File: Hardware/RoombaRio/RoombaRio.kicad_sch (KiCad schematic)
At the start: 1 part, among them J101 Raspberry_Pi_2_3

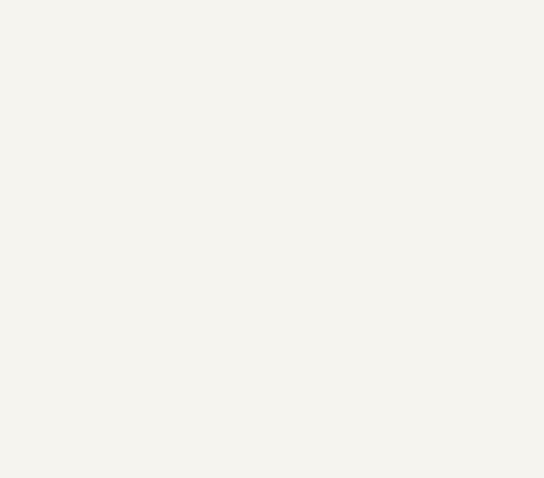
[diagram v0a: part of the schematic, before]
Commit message: Layout the basic roomba plug symbol
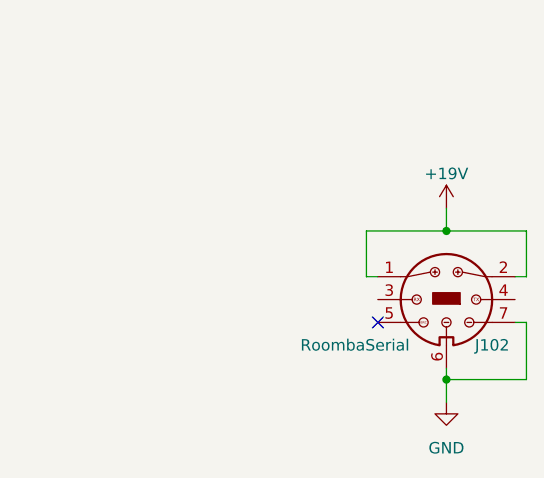
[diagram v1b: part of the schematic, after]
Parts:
- added J102: RoombaSerial, symbol KenwoodFox:RoombaSerial
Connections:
- new net +19V: J102.1, J102.2
- new net GND: J102.6, J102.7
- no-connect marks 0 -> 1
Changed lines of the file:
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@@
 (kicad_sch (version 20230121) (generator eeschema)
   (paper "A4")
+  (junction (at 228.6 130.81) (diameter 0) (color 0 0 0 0)
+  )
+  (junction (at 228.6 147.32) (diameter 0) (color 0 0 0 0)
+  )
+  (no_connect (at 220.98 140.97))
+  (wire (pts (xy 219.71 135.89) (xy 220.98 135.89))
+    (stroke (width 0) (type default))
+  )
+  (wire (pts (xy 228.6 147.32) (xy 228.6 149.86))
+    (stroke (width 0) (type default))
+  )
+  (wire (pts (xy 237.49 135.89) (xy 237.49 130.81))
+    (stroke (width 0) (type default))
+  )
+  (wire (pts (xy 236.22 135.89) (xy 237.49 135.89))
+    (stroke (width 0) (type default))
+  )
+  (wire (pts (xy 228.6 130.81) (xy 219.71 130.81))
+    (stroke (width 0) (type default))
+  )
+  (wire (pts (xy 228.6 128.27) (xy 228.6 130.81))
+    (stroke (width 0) (type default))
+  )
+  (wire (pts (xy 228.6 130.81) (xy 237.49 130.81))
+    (stroke (width 0) (type default))
+  )
+  (wire (pts (xy 237.49 140.97) (xy 237.49 147.32))
+    (stroke (width 0) (type default))
+  )
+  (wire (pts (xy 236.22 140.97) (xy 237.49 140.97))
+    (stroke (width 0) (type default))
+  )
+  (wire (pts (xy 228.6 147.32) (xy 237.49 147.32))
+    (stroke (width 0) (type default))
+  )
+  (wire (pts (xy 228.6 146.05) (xy 228.6 147.32))
+    (stroke (width 0) (type default))
+  )
+  (wire (pts (xy 219.71 130.81) (xy 219.71 135.89))
+    (stroke (width 0) (type default))
+  )
+  (symbol (lib_id "power:GND") (at 228.6 149.86 0) (unit 1)
+    (in_bom yes) (on_board yes) (dnp no) (fields_autoplaced)
+    (property "Reference" "#PWR0101" (at 228.6 156.21 0)
+      (effects (font (size 1.27 1.27)) hide)
+    )
+    (property "Value" "GND" (at 228.6 154.94 0)
+      (effects (font (size 1.27 1.27)))
+    )
+    (property "Footprint" "" (at 228.6 149.86 0)
+      (effects (font (size 1.27 1.27)) hide)
+    )
+    (property "Datasheet" "" (at 228.6 149.86 0)
+      (effects (font (size 1.27 1.27)) hide)
+    )
+    (pin "1")
+    (instances
+      (project "RoombaRio"
+        (path "/88f1b535-e503-4390-8d17-9a3e3042362a"
+          (reference "#PWR0101") (unit 1)
+        )
+      )
+    )
+  )
   (symbol (lib_id "Connector:Raspberry_Pi_2_3") (at 145.415 100.965 0) (unit 1)
     (in_bom yes) (on_board yes) (dnp no) (fields_autoplaced)
@@
         )
       )
+    )
+  )
+  (symbol (lib_id "KenwoodFox:+19V") (at 228.6 128.27 0) (unit 1)
+    (in_bom yes) (on_board yes) (dnp no) (fields_autoplaced)
+    (property "Reference" "#PWR0102" (at 228.6 132.08 0)
+      (effects (font (size 1.27 1.27)) hide)
+    )
+    (property "Value" "+19V" (at 228.6 124.46 0)
+      (effects (font (size 1.27 1.27)))
+    )
+    (property "Footprint" "" (at 228.6 128.27 0)
+      (effects (font (size 1.27 1.27)) hide)
+    )
+    (property "Datasheet" "" (at 228.6 128.27 0)
+      (effects (font (size 1.27 1.27)) hide)
+    )
+    (pin "1")
+    (instances
+      (project "RoombaRio"
+        (path "/88f1b535-e503-4390-8d17-9a3e3042362a"
+          (reference "#PWR0102") (unit 1)
+        )
+      )
+    )
+  )
+  (symbol (lib_id "KenwoodFox:RoombaSerial") (at 228.6 138.43 180) (unit 1)
+    (in_bom yes) (on_board yes) (dnp no)
+    (property "Reference" "J102" (at 233.68 143.51 0)
+      (effects (font (size 1.27 1.27)))
+    )
+    (property "Value" "RoombaSerial" (at 218.44 143.51 0)
+      (effects (font (size 1.27 1.27)))
+    )
+    (property "Footprint" "" (at 228.6 138.43 0)
+      (effects (font (size 1.27 1.27)) hide)
+    )
+    (property "Datasheet" "" (at 228.6 138.43 0)
+      (effects (font (size 1.27 1.27)) hide)
+    )
+    (pin "1")
+    (pin "2")
+    (pin "3")
+    (pin "4")
+    (pin "5")
+    (pin "6")
+    (pin "7")
+    (instances
+      (project "RoombaRio"
+        (path "/88f1b535-e503-4390-8d17-9a3e3042362a"
+          (reference "J102") (unit 1)
+        )
+      )

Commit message: Add inital edge cuts and upstream roomba improvements
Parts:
- J102: footprint (none) -> KenwoodFox:Roomba7Pin
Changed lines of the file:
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@@
       (effects (font (size 1.27 1.27)))
     )
-    (property "Footprint" "" (at 228.6 138.43 0)
+    (property "Footprint" "KenwoodFox:Roomba7Pin" (at 228.6 138.43 0)
       (effects (font (size 1.27 1.27)) hide)
     )

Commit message: Inital power mgmnt
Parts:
- added C101: 10uf, Capacitor_SMD:CP_Elec_4x3, symbol Device:C_Polarized_Small
- added C102: 100nF, Capacitor_SMD:C_0805_2012Metric, symbol Device:C_Small
- added C103: 1uF, Capacitor_SMD:C_0805_2012Metric, symbol Device:C_Small
- added D101: PWR, LED_SMD:LED_0805_2012Metric, symbol Device:LED
- added R101: 2.2K, Resistor_SMD:R_0805_2012Metric, symbol Device:R_Small
- added U101: AMS1117CD, Package_TO_SOT_SMD:TO-252-3_TabPin2, symbol Regulator_Linear:AMS1117CD
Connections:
- net GND: now also J101.14 (GND), J101.20 (GND), J101.25 (GND), J101.30 (GND), J101.34 (GND), J101.39 (GND), J101.6 (GND), J101.9 (GND), C101.2, C102.2, C103.2, D101.1 (K)
- net +3V3: now reaches J101.1 (3V3)
- net +3V3: now also J101.17 (3V3)
- net +5V: now reaches J101.2 (5V)
- net +5V: now also J101.4 (5V), C102.1, C103.1, R101.1, U101.2 (VO)
- net ROOMBA_RX: now reaches J102.3
- net ROOMBA_TX: now reaches J102.4
- net ROOMBA_BRC: now reaches J102.5
- net +19V renamed +BATT
- net +BATT: now also C101.1, U101.3 (VI)
- new net: D101.2 (A), R101.2

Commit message: off to robotics
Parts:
- added J103: i2c Header, Connector_JST:JST_XH_S4B-XH-A_1x04_P2.50mm_Horizontal, symbol Connector:Conn_01x04_Pin
- added J104: GPIO, Connector_JST:JST_XH_S6B-XH-A_1x06_P2.50mm_Horizontal, symbol Connector:Conn_01x06_Pin
- added Q101, Q102: BSS138, Package_TO_SOT_SMD:SOT-23, symbol Transistor_FET:BSS138
- added Q103: DNF, Package_TO_SOT_SMD:SOT-23, symbol Transistor_FET:BSS138
- added R102, R103, R104, R105: 10k, Resistor_SMD:R_0805_2012Metric, symbol Device:R_Small
- added R106, R107: DNF, Resistor_SMD:R_0805_2012Metric, symbol Device:R_Small
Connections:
- net +3V3: now also J103.4 (Pin_4), Q101.1 (G), Q102.1 (G), Q103.1 (G), R102.2, R104.2, R106.2
- net +5V: now also R103.2, R105.2, R107.2
- net GND: now also J103.1 (Pin_1), J104.1 (Pin_1)
- net ROOMBA_BRC: now also Q103.3 (D), R107.1
- net ROOMBA_RX: now also Q101.3 (D), R103.1
- net ROOMBA_TX: now also Q102.3 (D), R105.1
- net PI_RX: now reaches J101.10 (GPIO15/RXD)
- net PI_RX: now also Q102.2 (S), R104.1
- net GPIO10: now reaches J101.19 (MOSI0/GPIO10)
- net GPIO10: now also J104.5 (Pin_5)
- net GPIO9: now reaches J101.21 (MISO0/GPIO9)
- net GPIO9: now also J104.4 (Pin_4)
- net GPIO11: now reaches J101.23 (SCLK0/GPIO11)
- net GPIO11: now also J104.6 (Pin_6)
- net GPIO0: now reaches J101.27 (ID_SD/GPIO0)
- net GPIO0: now also J104.2 (Pin_2)
- net GPIO1: now reaches J101.28 (ID_SC/GPIO1)
- net GPIO1: now also J104.3 (Pin_3)
- net SDA: now reaches J101.3 (SDA/GPIO2)
- net SDA: now also J103.2 (Pin_2)
- net SCL: now reaches J101.5 (SCL/GPIO3)
- net SCL: now also J103.3 (Pin_3)
- net PI_TX: now reaches J101.8 (GPIO14/TXD)
- net PI_TX: now also Q101.2 (S), R102.1
- new net PI_BRC: Q103.2 (S), R106.1
- no-connect marks 1 -> 8
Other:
- moved on the sheet: J101
